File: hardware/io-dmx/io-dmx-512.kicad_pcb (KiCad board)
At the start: 2 copper layers, 68.6 x 53.3 mm, 20 parts, among them J1 Input

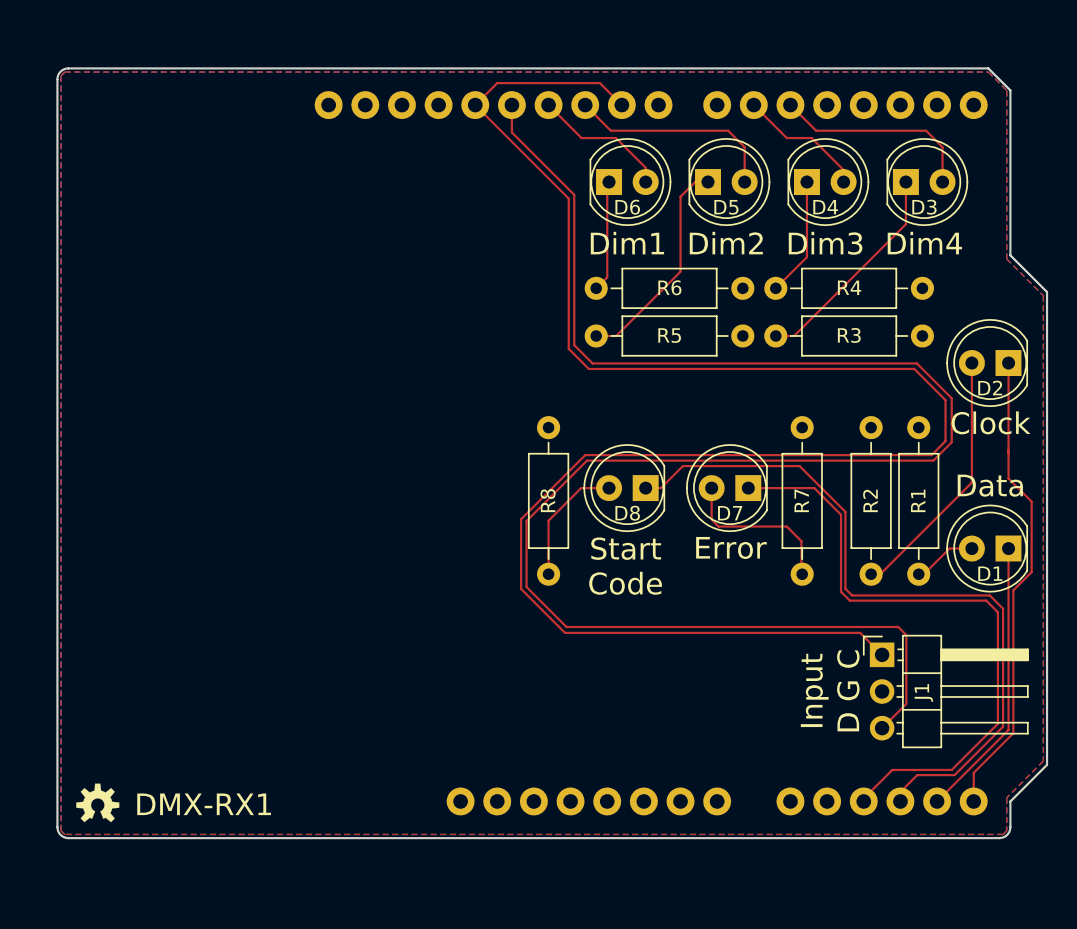
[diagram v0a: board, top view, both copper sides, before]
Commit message: Prototype version of DMX, Analog, and PWM IO Modules and both TX and RX IO interfaces.
Make io-analog a stackable family
io-analog-core handles D to A
io-analog-voltage handles voltage output
io-analog-pwm handles pwm output for leds, drive display pro

Refactor display-pro to work with io-analog-pwm
Add correct coax power connector

Move TX2 to tx-io
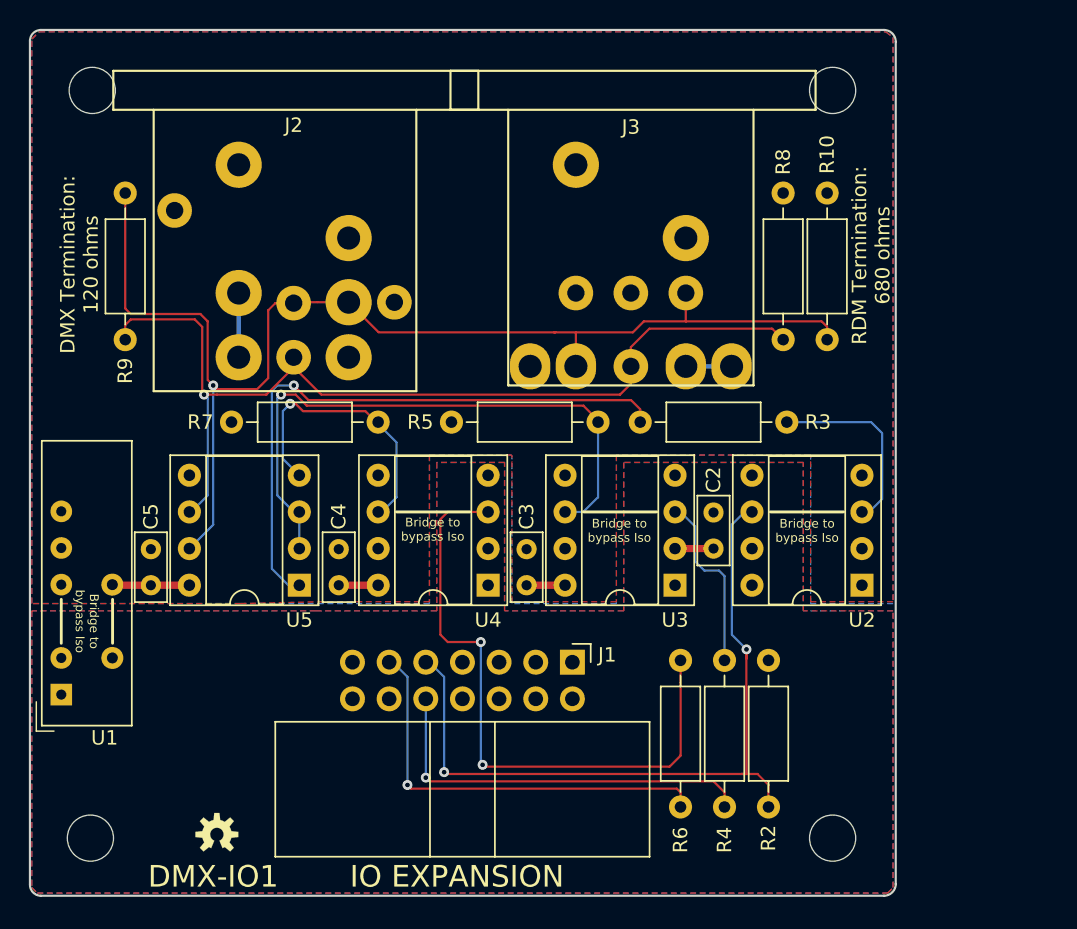
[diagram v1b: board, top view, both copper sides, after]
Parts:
- removed A1: Arduino_UNO_R3, footprints:ARDUINO_R3_NO_HOLES
- removed D1: DATA, LED_THT:LED_D5.0mm
- removed D2: CLOCK, LED_THT:LED_D5.0mm
- removed D3: DIM3, LED_THT:LED_D5.0mm
- removed D4: DIM2, LED_THT:LED_D5.0mm
- removed D5: DIM1, LED_THT:LED_D5.0mm
- removed D6: DIM0, LED_THT:LED_D5.0mm
- removed D7: ERROR, LED_THT:LED_D5.0mm
- removed D8: START_CODE, LED_THT:LED_D5.0mm
- removed R1: 330, Resistor_THT:R_Axial_DIN0207_L6.3mm_D2.5mm_P10.16mm_Horizontal
- added C2: .01uF, Capacitor_THT:C_Rect_L4.6mm_W2.0mm_P2.50mm_MKS02_FKP02, F.Cu at (161.8, 96.5)
- added C3: .01uF, Capacitor_THT:C_Rect_L4.6mm_W2.0mm_P2.50mm_MKS02_FKP02, F.Cu at (148.8, 99.1)
- added C4: .01uF, Capacitor_THT:C_Rect_L4.6mm_W2.0mm_P2.50mm_MKS02_FKP02, F.Cu at (135.8, 99.1)
- added C5: .01uF, Capacitor_THT:C_Rect_L4.6mm_W2.0mm_P2.50mm_MKS02_FKP02, F.Cu at (122.8, 99.1)
- added J2: NC3FAH/NC5FAH, footprints:NEUTRIK-NC3FAH-NC5FAH, F.Cu at (132.7, 66.1)
- added J3: NC3MAH/NC5MAH, footprints:NEUTRIK-NC3MAH-NC5MAH, F.Cu at (156.1, 66.1)
- added MH1: MountingHole, MountingHole:MountingHole_3.2mm_M3, F.Cu at (118.7, 64.8)
- added MH2: MountingHole, MountingHole:MountingHole_3.2mm_M3, F.Cu at (170.1, 64.8)
- added MH3: MountingHole, MountingHole:MountingHole_3.2mm_M3, F.Cu at (118.6, 116.6)
- added MH4: MountingHole, MountingHole:MountingHole_3.2mm_M3, F.Cu at (170.1, 116.6)
- added R10: 680, Resistor_THT:R_Axial_DIN0207_L6.3mm_D2.5mm_P10.16mm_Horizontal, F.Cu at (169.7, 82.0)
- added R9: 120, Resistor_THT:R_Axial_DIN0207_L6.3mm_D2.5mm_P10.16mm_Horizontal, F.Cu at (121.0, 71.9)
- added U1: NMA0505SC, footprints:Converter_DCDC_muRata_NMAxxxxSC_THT_Bypass, F.Cu at (116.6, 106.6)
- added U2: 6N137, Package_DIP:DIP-8_W7.62mm_Socket, F.Cu at (172.1, 99.1)
- added U3: 6N137, Package_DIP:DIP-8_W7.62mm_Socket, F.Cu at (159.1, 99.1)
- added U4: 6N137, Package_DIP:DIP-8_W7.62mm_Socket, F.Cu at (146.2, 99.1)
- added U5: MAX3485CPA+, Package_DIP:DIP-8_W7.62mm_Socket, F.Cu at (133.1, 99.1)
- J1: value Input -> IO EXTENSION; footprint Connector_PinHeader_2.54mm:PinHeader_1x03_P2.54mm_Horizontal -> Connector_IDC:IDC-Header_2x07_P2.54mm_Horizontal
- R2, R3, R4, R5, R6, R7: value 330 -> 470
- R8: value 330 -> 680
- moved R7 29.4 mm to (138.6, 87.8), turned to 180 degrees
- moved R4 29.2 mm to (162.6, 104.3), turned to 270 degrees
- moved R6 26.1 mm to (159.5, 104.3), turned to 270 degrees
- moved J1 21.5 mm to (152.0, 104.4), turned to 270 degrees
- moved R3 20.4 mm to (156.7, 87.8), turned to 0 degrees
- moved R2 17.6 mm to (165.6, 104.3)
- moved R8 17.4 mm to (166.6, 82.0), turned to 90 degrees
- moved G*** 15.5 mm to (133.9, 116.6)
- moved R5 11.7 mm to (153.8, 87.8)
- moved ? 8.50 mm to (127.4, 116.3)
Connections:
- J1 pad 1: /RXCLK -> +5V
- J1 pad 2: GND -> +5V
- J1 pad 3: /RX -> Net-(J1-Pad3)
- R2 pad 2: Net-(D2-Pad2) -> /DMX-RX
- R3 pad 1: GND -> Net-(R3-Pad1)
- R4 pad 1: GND -> Net-(R4-Pad1)
- R4 pad 2: Net-(D4-Pad1) -> /DMX-DIR
- R5 pad 1: GND -> Net-(R5-Pad1)
- R5 pad 2: Net-(D5-Pad1) -> VDD
- R6 pad 1: GND -> Net-(R6-Pad1)
- R6 pad 2: Net-(D6-Pad1) -> /DMX-TX
- R7 pad 1: +5V -> Net-(R7-Pad1)
- R7 pad 2: Net-(D7-Pad2) -> VDD
- R8 pad 1: +5V -> Net-(J2-Pad3)
- R8 pad 2: Net-(D8-Pad2) -> VDD
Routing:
- net /RXCLK: track 126.2 -> 0.00 mm
- net /RX: track 120.3 -> 0.00 mm
- net Net-(J2-Pad2A): track 0.00 -> 87.4 mm, vias 0 -> 1
- net Net-(J2-Pad3): track 0.00 -> 67.1 mm, vias 0 -> 1
- net /DMX-RX: track 0.00 -> 53.0 mm, vias 0 -> 2
- net /~SC: track 50.4 -> 0.00 mm
- net Net-(R6-Pad1): track 0.00 -> 43.8 mm, vias 0 -> 2
- net /~ERR: track 43.4 -> 0.00 mm
- net Net-(R5-Pad1): track 0.00 -> 42.4 mm, vias 0 -> 1
- net Net-(R3-Pad1): track 0.00 -> 42.0 mm, vias 0 -> 1
- net /~CLOCK: track 33.0 -> 0.00 mm
- net /DMX-TX: track 0.00 -> 29.3 mm, vias 0 -> 1
- net /DMX-DIR: track 0.00 -> 27.6 mm, vias 0 -> 1
- net Net-(R7-Pad1): track 0.00 -> 19.7 mm, vias 0 -> 1
- net /~DATA: track 19.6 -> 0.00 mm
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- added copper zone on B.Cu, net GNDD
- added copper zone on F.Cu, net VDD
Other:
- board size 68.6 x 53.3 mm -> 60 x 60 mm
- board text added: "Bridge to bypass Iso"
- board text added: "DMX Termination: 120 ohms"
- board text added: "DMX-IO1"
- board text added: "DMX-IO1, Rev 1.2 Crazy Giraffe Software"
- board text added: "IO EXPANSION"
- board text added: "RDM Termination: 680 ohms"
- board text removed: "Clock"
- board text removed: "D G C"
- board text removed: "DMX-RX1"
- board text removed: "DMX-RX1, Rev 1.3 Crazy Giraffe Software"
- board text removed: "Data"
- board text removed: "Dim1"
- board text removed: "Dim2"
- board text removed: "Dim3"
- board text removed: "Dim4"
- board text removed: "Error"
- board text removed: "Input"
- board text removed: "Start Code"
